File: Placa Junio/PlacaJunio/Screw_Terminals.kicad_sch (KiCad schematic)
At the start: 16 parts, among them J3 Terminal Paracaidas 2, J4 Terminal Paracaidas 1, J5 Terminal Paracaidas 3, J6 Terminal Paracaidas 4, Q2 IRLML0030, Q3 IRLML0030, Q5 IRLML0030, Q6 IRLML0030

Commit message: Cambios
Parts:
- removed R11, R13, R6, R8: 4.7 Ohm, 2.5W max, Resistor_THT:R_Axial_DIN0204_L3.6mm_D1.6mm_P2.54mm_Vertical, symbol Device:R
- added R14, R16, R17, R20: 1, Resistor_SMD:R_0402_1005Metric, symbol Device:R
- added R15, R18, R19, R21: 1M, Resistor_SMD:R_0402_1005Metric, symbol Device:R
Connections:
- net +3V3: now also J3.1 (Pin_1), J4.1 (Pin_1), J5.1 (Pin_1), J6.1 (Pin_1)
- net GND: now also R15.2, R18.2, R19.2, R21.2
- net at Q5.3 (D): now also R16.2; no longer J5.2 (Pin_2)
- net at Q3.3 (D): now also R14.2; no longer J4.2 (Pin_2)
- net at Q2.3 (D): now also R17.2; no longer J3.2 (Pin_2)
- net at Q6.3 (D): now also R20.2; no longer J6.2 (Pin_2)
- new net SENSE1: J4.2 (Pin_2), R14.1, R15.1
- new net SENSE2: J3.2 (Pin_2), R17.1, R18.1
- new net SENSE3: J5.2 (Pin_2), R16.1, R19.1
- new net SENSE4: J6.2 (Pin_2), R20.1, R21.1
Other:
- moved on the sheet: Q2, Q3, Q5, Q6, R10, R12, R5, R7

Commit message: Update Screw_Terminals.kicad_sch
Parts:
- J3: value Terminal Paracaidas 2 -> Terminal P2
- J4: value Terminal Paracaidas 1 -> Terminal P1
- J5: value Terminal Paracaidas 3 -> Terminal P3
- J6: value Terminal Paracaidas 4 -> Terminal P4
- R14, R16, R17, R20: value 1 -> 3.3 Ohm 1%; footprint Resistor_SMD:R_0402_1005Metric -> Resistor_SMD:R_0805_2012Metric; Nº Componente (none) -> RCS08053R30FKEA
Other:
- moved on the sheet: J3, J4, J5, J6, Q2, Q3, Q5, Q6, R10, R12, R14, R15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

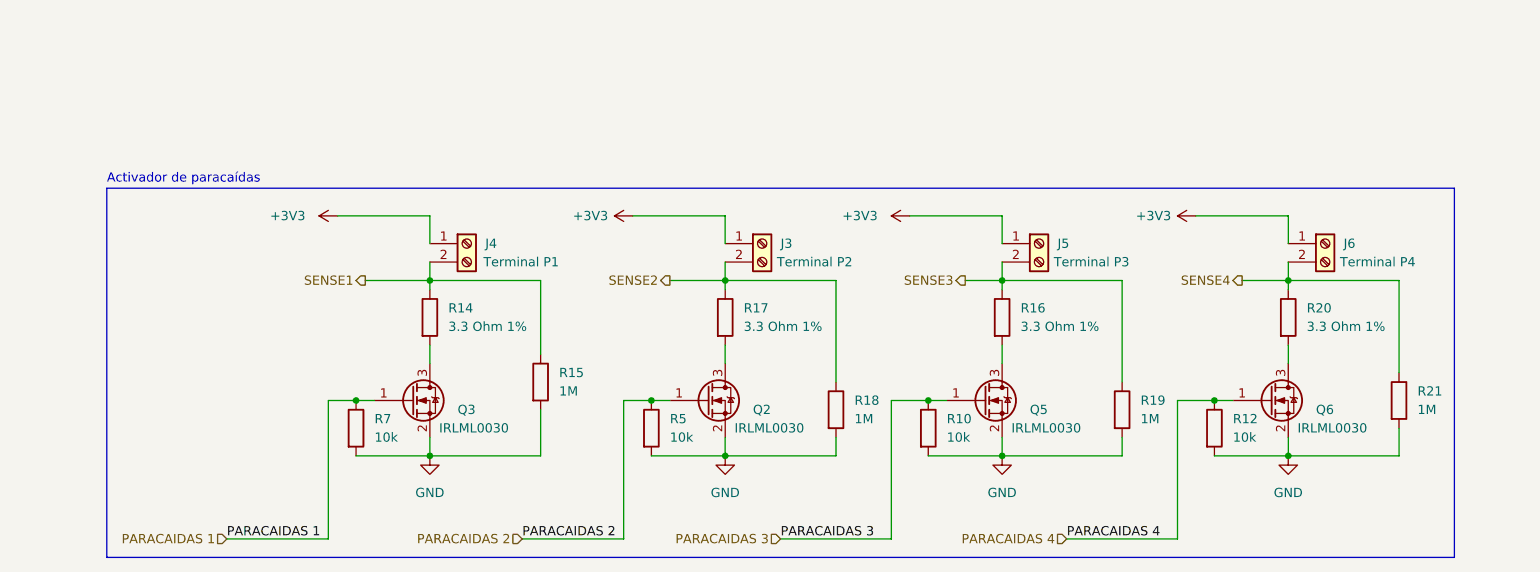
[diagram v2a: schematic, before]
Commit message: Elementos posicionados
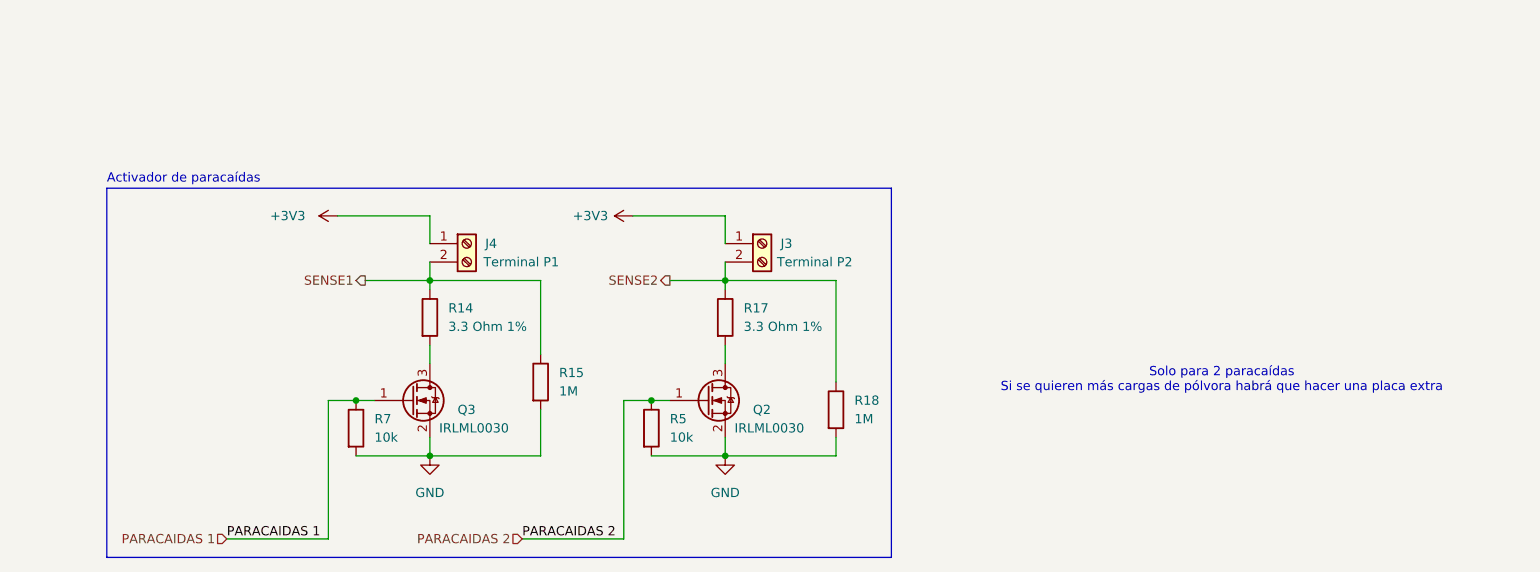
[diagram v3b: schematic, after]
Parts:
- removed J5: Terminal P3, TerminalBlock:TerminalBlock_bornier-2_P5.08mm, symbol Connector:Screw_Terminal_01x02
- removed J6: Terminal P4, TerminalBlock:TerminalBlock_bornier-2_P5.08mm, symbol Connector:Screw_Terminal_01x02
- removed Q5, Q6: IRLML0030, Package_TO_SOT_SMD:SOT-23, symbol Transistor_FET:IRLML0030
- removed R10, R12: 10k, Resistor_SMD:R_0402_1005Metric, symbol Device:R
- removed R16, R20: 3.3 Ohm 1%, Resistor_SMD:R_0805_2012Metric, symbol Device:R
- removed R19, R21: 1M, Resistor_SMD:R_0402_1005Metric, symbol Device:R
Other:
- note added: "Solo para 2 paracaídas Si se quieren más cargas de pólvora habrá que hacer una placa extra"
